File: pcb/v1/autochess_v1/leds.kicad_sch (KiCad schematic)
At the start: 128 parts

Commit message: Finish the schematic draft, start pcb layout
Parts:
- C1, C10, C11, C12, C13, C14, C15, C16, C17, C18, C19, C2, C20, C21, C22, C23, C24, C25, C26, C27, C28, C29, C3, C30, C31, C32, C33, C34, C35, C36, C37, C38, C39, C4, C40, C41, C42, C43, C44, C45, C46, C47, C48, C49, C5, C50, C51, C52, C53, C54, C55, C56, C57, C58, C59, C6, C60, C61, C62, C63, C64, C7, C8, C9: footprint (none) -> Capacitor_SMD:C_1206_3216Metric_Pad1.33x1.80mm_HandSolder

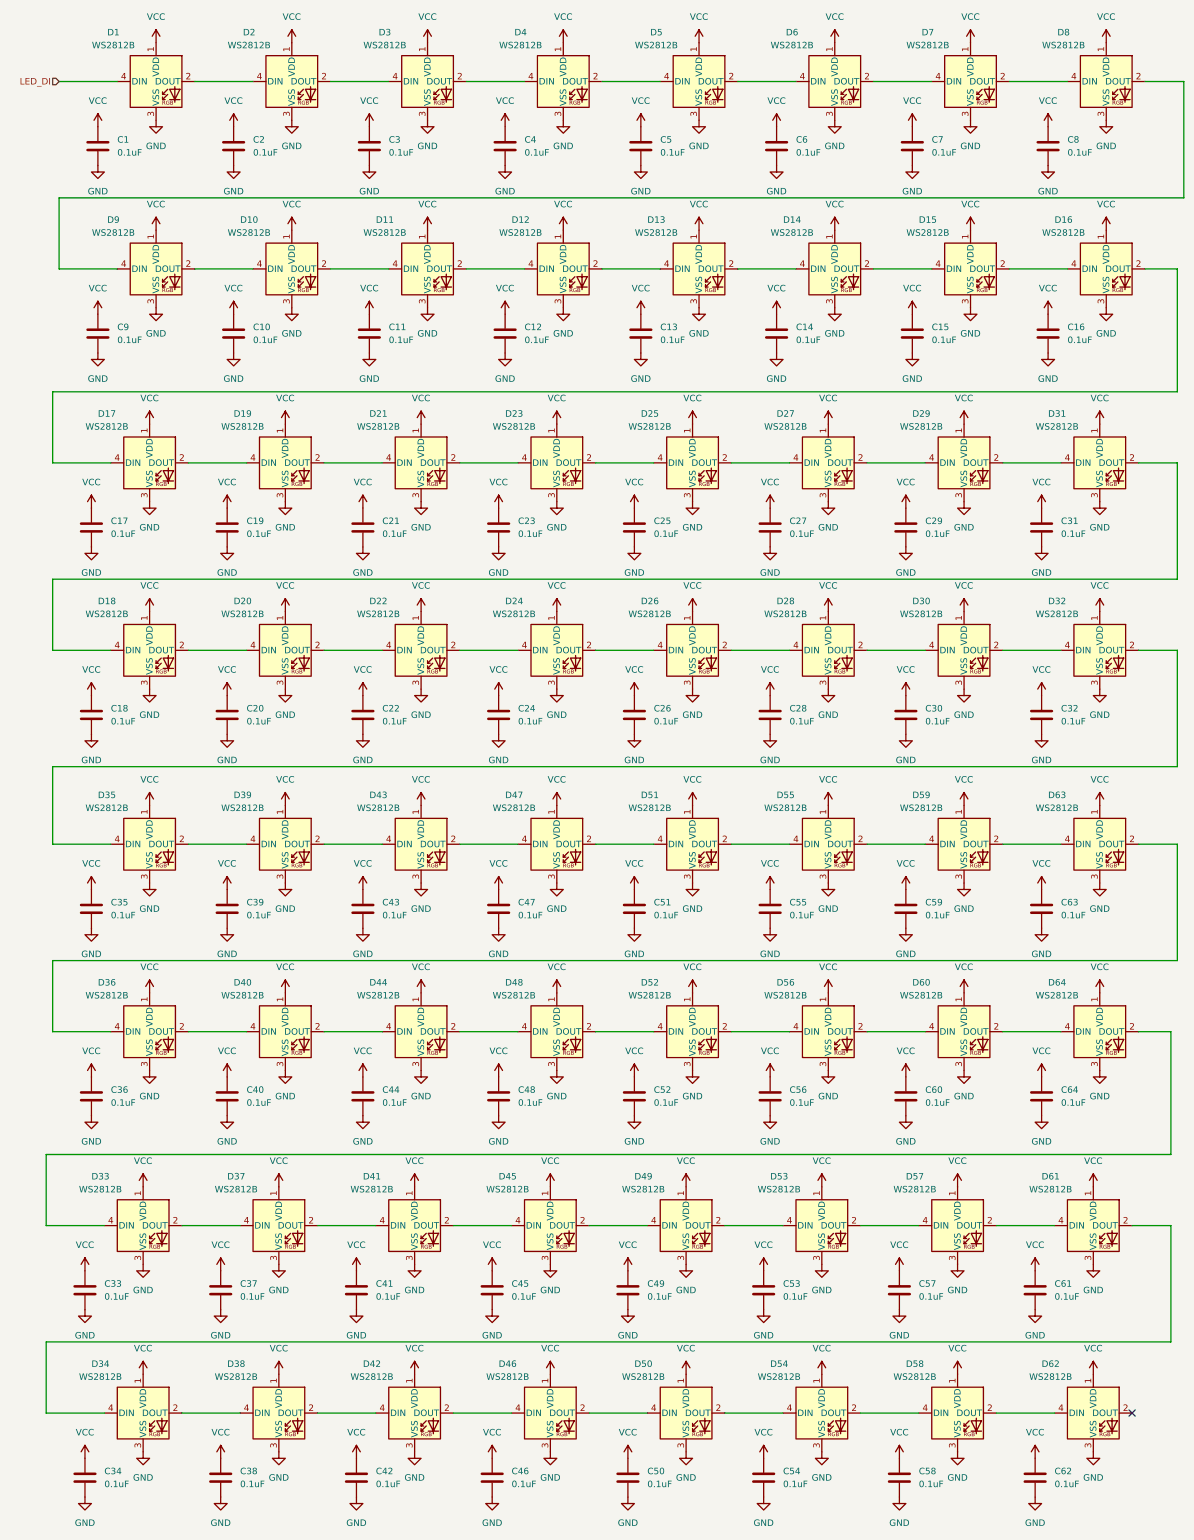
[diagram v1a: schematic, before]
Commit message: Continue laying out the PCB
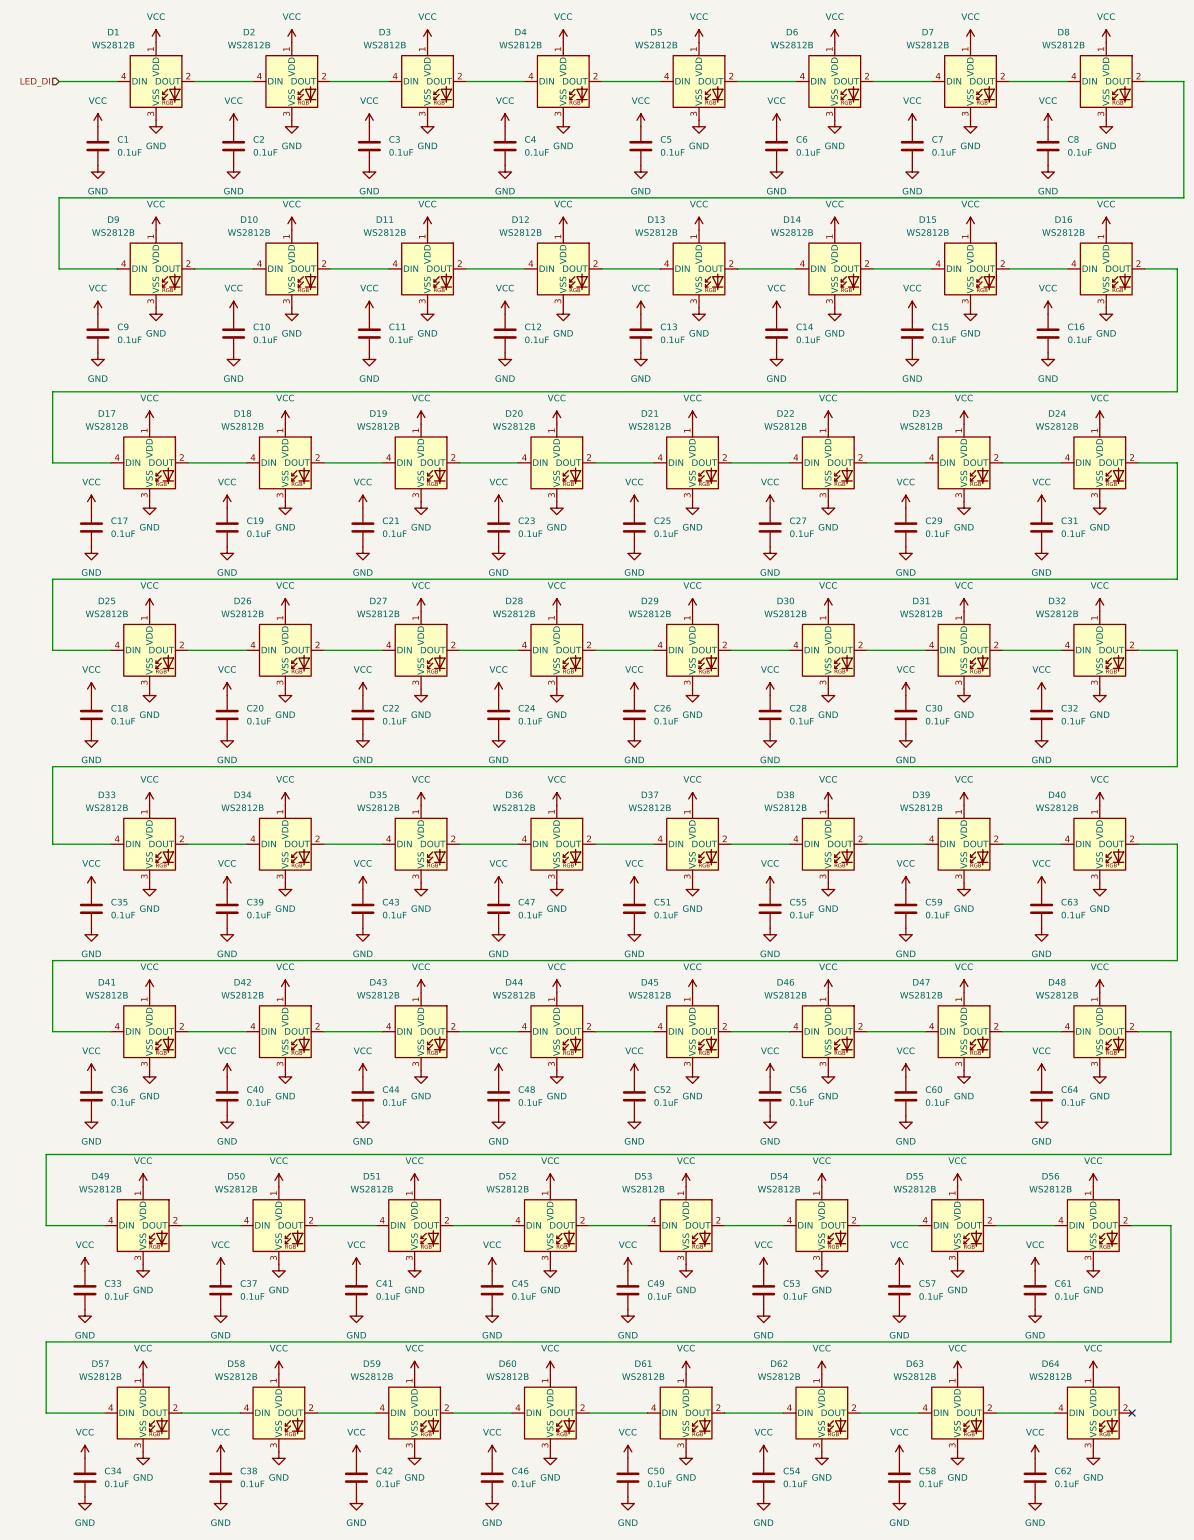
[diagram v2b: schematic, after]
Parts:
- renumbered D19 to D18, D21 to D19, D23 to D20, D25 to D21, D27 to D22, D29 to D23, D31 to D24, D18 to D25, D20 to D26, D22 to D27, D24 to D28, D26 to D29, D28 to D30, D30 to D31, D35 to D33, D39 to D34, D43 to D35, D47 to D36, D51 to D37, D55 to D38, D59 to D39, D63 to D40, D36 to D41, D40 to D42, D44 to D43, D48 to D44, D52 to D45, D56 to D46, D60 to D47, D64 to D48, D33 to D49, D37 to D50, D41 to D51, D45 to D52, D49 to D53, D53 to D54, D57 to D55, D61 to D56, D34 to D57, D38 to D58, D42 to D59, D46 to D60, D50 to D61, D54 to D62, D58 to D63, D62 to D64
